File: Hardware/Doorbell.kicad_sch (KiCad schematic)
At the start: 57 parts, among them J1 Conn_02x05_Odd_Even, J2 MEM2051-00-195-00-A, J3 1935174, Q1 SIA517DJ-T1-GE3, Q2 DMP4047LFDE-7, U1 CD4052BPWRG3, U2 MAX98357AETE+T, U3 ATSAMG53N19B-AU, U4 VOS627A-X001T, U5 VOS627A-X001T, U6 MR25H128A

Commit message: Clean up custom KiCad libraries
- Clean up the directory structure for KiCad custom libraries.
- Fix paths in KiCad schematic and pcb for symbols, footprints, and
3d models for custom libraries.
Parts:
- F1, F2: footprint Libs:FUSE_4527 -> Fuse:FUSE_4527
- J1: footprint Libs:3220-10-0100-00 -> Connector:3220-10-0100-00
- J2: footprint Libs:MEM2051-00-195-00-A -> Connector:MEM2051-00-195-00-A
- Q2: footprint Libs:DMP4047LFDE-7 -> Transistor_SMD:DMP4047LFDE-7
- R10, R9: footprint Libs:35501K3FT -> Resistor_SMD:35501K3FT
- RV2: footprint Libs:PTV09A-4015U-B103 -> Potentiometer:PTV09A-4015U-B103
- U2: footprint Libs:MAX98357AETE_T -> IC:MAX98357AETE_T
- U3: footprint Libs:ATSAMG53N19B-AU -> IC:ATSAMG53N19B-AU
- U4, U5: footprint Libs:VOS627A-X001T -> IC:VOS627A-X001T

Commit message: Cleanup custom KiCad libraries
- Delete unneeded/unused files
- Cleanup symbol library files for custom libraries
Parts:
- J2: symbol MEM2051-00-195-00-A:MEM2051-00-195-00-A -> Doorbell_Connector:MEM2051-00-195-00-A
- Q1: symbol SIA517DJ-T1-GE3:SIA517DJ-T1-GE3 -> Doorbell_Transistor_SMD:SIA517DJ-T1-GE3
- Q2: symbol DMP4047LFDE-7:DMP4047LFDE-7 -> Doorbell_Transistor_SMD:DMP4047LFDE-7
- RV2: symbol PTV09A-4015U-B103:PTV09A-4015U-B103 -> Doorbell_Potentiometer:PTV09A-4015U-B103
- U1: symbol CD4052BPWRG3:CD4052BPWRG3 -> Doorbell_IC:CD4052BPWRG3
- U2: symbol MAX98357AETE_T:MAX98357AETE+T -> Doorbell_IC:MAX98357AETE+T
- U3: symbol ATSAMG53N19B-AU:ATSAMG53N19B-AU -> Doorbell_IC:ATSAMG53N19B-AU
- U4, U5: symbol VOS627A-X001T:VOS627A-X001T -> Doorbell_IC:VOS627A-X001T
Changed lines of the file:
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@@
     (pin "2")
   )
-  (symbol (lib_id "MAX98357AETE_T:MAX98357AETE+T") (at 83.82 156.21 0) (unit 1)
+  (symbol (lib_id "Doorbell_IC:MAX98357AETE+T") (at 83.82 156.21 0) (unit 1)
     (in_bom yes) (on_board yes)
     (property "Reference" "U2" (id 0) (at 83.82 136.652 0))
@@
     (pin "2")
   )
-  (symbol (lib_id "SIA517DJ-T1-GE3:SIA517DJ-T1-GE3") (at 77.47 116.84 0) (mirror y) (unit 2)
+  (symbol (lib_id "Doorbell_Transistor_SMD:SIA517DJ-T1-GE3") (at 77.47 116.84 0) (mirror y) (unit 2)
     (in_bom yes) (on_board yes)
     (property "Reference" "Q1" (id 0) (at 74.803 115.6716 0)
@@
     (pin "5")
   )
-  (symbol (lib_id "SIA517DJ-T1-GE3:SIA517DJ-T1-GE3") (at 55.88 102.87 180) (unit 1)
+  (symbol (lib_id "Doorbell_Transistor_SMD:SIA517DJ-T1-GE3") (at 55.88 102.87 180) (unit 1)
     (in_bom yes) (on_board yes)
     (property "Reference" "Q1" (id 0) (at 53.213 101.7016 0)
@@
     (pin "1")
   )
-  (symbol (lib_id "CD4052BPWRG3:CD4052BPWRG3") (at 46.99 63.5 90) (unit 1)
+  (symbol (lib_id "Doorbell_IC:CD4052BPWRG3") (at 46.99 63.5 90) (unit 1)
     (in_bom yes) (on_board yes)
     (property "Reference" "U1" (id 0) (at 28.1178 62.3316 90)
@@
     (pin "2")
   )
-  (symbol (lib_id "ATSAMG53N19B-AU:ATSAMG53N19B-AU") (at 161.29 97.79 0) (unit 1)
+  (symbol (lib_id "Doorbell_IC:ATSAMG53N19B-AU") (at 161.29 97.79 0) (unit 1)
     (in_bom yes) (on_board yes)
     (property "Reference" "U3" (id 0) (at 161.29 43.5102 0)
@@
     (pin "1")
   )
-  (symbol (lib_id "MEM2051-00-195-00-A:MEM2051-00-195-00-A") (at 248.92 38.1 180) (unit 1)
+  (symbol (lib_id "Doorbell_Connector:MEM2051-00-195-00-A") (at 248.92 38.1 180) (unit 1)
     (in_bom yes) (on_board yes)
     (property "Reference" "J2" (id 0) (at 244.0178 18.6182 0))
@@
     (pin "9")
   )
-  (symbol (lib_id "PTV09A-4015U-B103:PTV09A-4015U-B103") (at 99.06 88.9 0) (unit 1)
+  (symbol (lib_id "Doorbell_Potentiometer:PTV09A-4015U-B103") (at 99.06 88.9 0) (unit 1)
     (in_bom yes) (on_board yes)
     (property "Reference" "RV2" (id 0) (at 97.5614 86.5886 0)
@@
     (pin "1")
   )
-  (symbol (lib_id "VOS627A-X001T:VOS627A-X001T") (at 214.63 157.48 180) (unit 1)
+  (symbol (lib_id "Doorbell_IC:VOS627A-X001T") (at 214.63 157.48 180) (unit 1)
     (in_bom yes) (on_board yes)
     (property "Reference" "U5" (id 0) (at 214.63 148.082 0))
@@
     (pin "4")
   )
-  (symbol (lib_id "VOS627A-X001T:VOS627A-X001T") (at 214.63 132.08 0) (mirror y) (unit 1)
+  (symbol (lib_id "Doorbell_IC:VOS627A-X001T") (at 214.63 132.08 0) (mirror y) (unit 1)
     (in_bom yes) (on_board yes)
     (property "Reference" "U4" (id 0) (at 214.63 122.682 0))
@@
     (pin "2")
   )
-  (symbol (lib_id "DMP4047LFDE-7:DMP4047LFDE-7") (at 58.42 24.13 90) (unit 1)
+  (symbol (lib_id "Doorbell_Transistor_SMD:DMP4047LFDE-7") (at 58.42 24.13 90) (unit 1)
     (in_bom yes) (on_board yes)
     (property "Reference" "Q2" (id 0) (at 58.42 15.4432 90))

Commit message: Switch to local libraries for KiCad schematic
- Move all KiCad schematic symbols into local libraries
- Fix KiCad schematic library links to point to local libraries
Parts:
- BT1: symbol Device:Battery -> Doorbell_Battery:Battery
- C1, C10, C11, C12, C13, C14, C15, C16, C17, C18, C19, C2, C3, C4, C5, C6, C7, C8, C9: symbol Device:C_Small -> Doorbell_Capacitor:C_Small
- D1: symbol Device:D_Zener_Small -> Doorbell_Diode:D_Zener_Small
- D2: symbol Device:LED -> Doorbell_LED:LED
- F1, F2: symbol Device:Fuse_Small -> Doorbell_Fuse:Fuse_Small
- FB1, FB2: symbol Device:Ferrite_Bead_Small -> Doorbell_Inductor_SMD:FerriteBead_Small
- J1: value Conn_02x05_Odd_Even -> 3220-10-0100-00; symbol Connector_Generic:Conn_02x05_Odd_Even -> Doorbell_Connector:3220-10-0100-00
- J3: footprint TerminalBlock_Phoenix:TerminalBlock_Phoenix_PT-1,5-3-5.0-H_1x03_P5.00mm_Horizontal -> Connector:TerminalBlock_Phoenix_PT-1,5-3-5.0-H_1x03_P5.00mm_Horizontal; symbol Connector:Screw_Terminal_01x03 -> Doorbell_Connector:Screw_Terminal_01x03
- LS1: symbol Device:Speaker -> Doorbell_Speaker:Speaker
- R1, R10, R11, R12, R13, R14, R15, R2, R3, R4, R5, R6, R7, R8, R9: symbol Device:R_Small -> Doorbell_Resistor:R_Small
- RV1, RV3, RV4: symbol Device:Varistor -> Doorbell_Varistor:Varistor
- U6: symbol Memory_NVRAM:MR25H40 -> Doorbell_Memory:MR25H40

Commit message: Move KiCad global footprint and 3d models to local
- Move KiCad global footprint and 3d models to local directories
- Reassign footprints in KiCad schematic/PCB from global libraries to
  local libraries
- Reassign global 3d models to local 3d models for KiCad
- Update KiCad PCB with all local footprints
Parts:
- BT1, LS1: footprint Connector_Molex:Molex_MicroClasp_55935-0210_1x02_P2.00mm_Horizontal -> Connector:Molex_MicroClasp_55935-0210_1x02_P2.00mm_Horizontal
- Q1: footprint Package_TO_SOT_SMD:Vishay_PowerPAK_SC70-6L_Dual -> Transistor_SMD:Vishay_PowerPAK_SC70-6L_Dual
- U1: footprint Package_SO:TSSOP-16_4.4x5mm_P0.65mm -> IC:TSSOP-16_4.4x5mm_P0.65mm
- U6: footprint Package_DFN_QFN:DFN-8-1EP_6x5mm_P1.27mm_EP2x2mm -> IC:DFN-8-1EP_6x5mm_P1.27mm_EP2x2mm
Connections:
- new net: U2.12 (NC), U2.13 (NC), U2.5 (NC), U2.6 (NC)
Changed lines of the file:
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@@
     (pin "8")
     (pin "9")
+    (pin "12")
+    (pin "13")
+    (pin "5")
+    (pin "6")
   )
   (symbol (lib_id "Doorbell_Capacitor:C_Small") (at 114.3 148.59 0) (unit 1)
@@
       (effects (font (size 1.27 1.27)) (justify left))
     )
-    (property "Footprint" "Connector_Molex:Molex_MicroClasp_55935-0210_1x02_P2.00mm_Horizontal" (id 2) (at 162.56 177.8 0)
+    (property "Footprint" "Connector:Molex_MicroClasp_55935-0210_1x02_P2.00mm_Horizontal" (id 2) (at 162.56 177.8 0)
       (effects (font (size 1.27 1.27)) hide)
     )
@@
       (effects (font (size 1.27 1.27)) (justify left))
     )
-    (property "Footprint" "Package_TO_SOT_SMD:Vishay_PowerPAK_SC70-6L_Dual" (id 2) (at 78.74 128.905 0)
+    (property "Footprint" "Transistor_SMD:Vishay_PowerPAK_SC70-6L_Dual" (id 2) (at 78.74 128.905 0)
       (effects (font (size 1.27 1.27)) hide)
     )
@@
       (effects (font (size 1.27 1.27)) (justify left))
     )
-    (property "Footprint" "Package_TO_SOT_SMD:Vishay_PowerPAK_SC70-6L_Dual" (id 2) (at 57.15 90.805 0)
+    (property "Footprint" "Transistor_SMD:Vishay_PowerPAK_SC70-6L_Dual" (id 2) (at 57.15 90.805 0)
       (effects (font (size 1.27 1.27)) hide)
     )
@@
       (effects (font (size 1.27 1.27)) (justify left))
     )
-    (property "Footprint" "Package_SO:TSSOP-16_4.4x5mm_P0.65mm" (id 2) (at 66.04 59.69 0)
+    (property "Footprint" "IC:TSSOP-16_4.4x5mm_P0.65mm" (id 2) (at 66.04 59.69 0)
       (effects (font (size 1.27 1.27)) (justify left) hide)
     )
@@
       (effects (font (size 1.27 1.27)) (justify left))
     )
-    (property "Footprint" "Connector_Molex:Molex_MicroClasp_55935-0210_1x02_P2.00mm_Horizontal" (id 2) (at 26.924 21.59 90)
+    (property "Footprint" "Connector:Molex_MicroClasp_55935-0210_1x02_P2.00mm_Horizontal" (id 2) (at 26.924 21.59 90)
       (effects (font (size 1.27 1.27)) hide)
     )
@@
     (property "Reference" "U6" (id 0) (at 250.19 58.9026 0))
     (property "Value" "MR25H128A" (id 1) (at 250.19 61.214 0))
-    (property "Footprint" "Package_DFN_QFN:DFN-8-1EP_6x5mm_P1.27mm_EP2x2mm" (id 2) (at 250.19 73.66 0)
+    (property "Footprint" "IC:DFN-8-1EP_6x5mm_P1.27mm_EP2x2mm" (id 2) (at 250.19 73.66 0)
       (effects (font (size 1.27 1.27)) hide)
     )
@@
     )
     (path "/00000000-0000-0000-0000-0000643f25be"
-      (reference "BT1") (unit 1) (value "6xAA") (footprint "Connector_Molex:Molex_MicroClasp_55935-0210_1x02_P2.00mm_Horizontal")
+      (reference "BT1") (unit 1) (value "6xAA") (footprint "Connector:Molex_MicroClasp_55935-0210_1x02_P2.00mm_Horizontal")
     )
     (path "/00000000-0000-0000-0000-00006195168d"
@@
     )
     (path "/00000000-0000-0000-0000-00006434f40f/00000000-0000-0000-0000-0000643d3326"
-      (reference "D6") (unit 1) (value "V3FM12-M3/H") (footprint "Diode_SMD:D_SMF")
+      (reference "D6") (unit 1) (value "V3FM12-M3/H") (footprint "Diode_SMD:V3FM12-M3_H")
     )
     (path "/00000000-0000-0000-0000-0000665129d9/00000000-0000-0000-0000-00006651647e"
@@
     )
     (path "/00000000-0000-0000-0000-0000619771f5"
-      (reference "LS1") (unit 1) (value "Speaker") (footprint "Connector_Molex:Molex_MicroClasp_55935-0210_1x02_P2.00mm_Horizontal")
+      (reference "LS1") (unit 1) (value "Speaker") (footprint "Connector:Molex_MicroClasp_55935-0210_1x02_P2.00mm_Horizontal")
     )
     (path "/00000000-0000-0000-0000-000061acc594"
-      (reference "Q1") (unit 1) (value "SIA517DJ-T1-GE3") (footprint "Package_TO_SOT_SMD:Vishay_PowerPAK_SC70-6L_Dual")
+      (reference "Q1") (unit 1) (value "SIA517DJ-T1-GE3") (footprint "Transistor_SMD:Vishay_PowerPAK_SC70-6L_Dual")
     )
     (path "/00000000-0000-0000-0000-000061ac7063"
-      (reference "Q1") (unit 2) (value "SIA517DJ-T1-GE3") (footprint "Package_TO_SOT_SMD:Vishay_PowerPAK_SC70-6L_Dual")
+      (reference "Q1") (unit 2) (value "SIA517DJ-T1-GE3") (footprint "Transistor_SMD:Vishay_PowerPAK_SC70-6L_Dual")
     )
     (path "/00000000-0000-0000-0000-0000675a9d90"
@@
     )
     (path "/00000000-0000-0000-0000-00006434f40f/00000000-0000-0000-0000-0000648f5004"
-      (reference "Q4") (unit 1) (value "BC847") (footprint "Package_TO_SOT_SMD:SOT-23")
+      (reference "Q4") (unit 1) (value "BC847") (footprint "Transistor_SMD:SOT-23")
     )
     (path "/00000000-0000-0000-0000-00006434f40f/00000000-0000-0000-0000-0000649028a0"
-      (reference "Q5") (unit 1) (value "BC847") (footprint "Package_TO_SOT_SMD:SOT-23")
+      (reference "Q5") (unit 1) (value "BC847") (footprint "Transistor_SMD:SOT-23")
     )
     (path "/00000000-0000-0000-0000-000061e3d0d7"
@@
     )
     (path "/00000000-0000-0000-0000-000061d6fed6"
-      (reference "U1") (unit 1) (value "CD4052BPWRG3") (footprint "Package_SO:TSSOP-16_4.4x5mm_P0.65mm")
+      (reference "U1") (unit 1) (value "CD4052BPWRG3") (footprint "IC:TSSOP-16_4.4x5mm_P0.65mm")
     )
     (path "/00000000-0000-0000-0000-00006194c427"
@@
     )
     (path "/00000000-0000-0000-0000-000066923e5d"
-      (reference "U6") (unit 1) (value "MR25H128A") (footprint "Package_DFN_QFN:DFN-8-1EP_6x5mm_P1.27mm_EP2x2mm")
+      (reference "U6") (unit 1) (value "MR25H128A") (footprint "IC:DFN-8-1EP_6x5mm_P1.27mm_EP2x2mm")
     )
     (path "/00000000-0000-0000-0000-00006434f40f/00000000-0000-0000-0000-000067503003"
@@
     )
     (path "/00000000-0000-0000-0000-00006434f40f/00000000-0000-0000-0000-00006757a4a0"
-      (reference "U9") (unit 1) (value "LM2903DR2G") (footprint "Package_SO:SOIC-8_3.9x4.9mm_P1.27mm")
+      (reference "U9") (unit 1) (value "LM2903DR2G") (footprint "IC:SOIC-8_3.9x4.9mm_P1.27mm")
     )
     (path "/00000000-0000-0000-0000-00006434f40f/00000000-0000-0000-0000-00006757cdae"
-      (reference "U9") (unit 2) (value "LM2903DR2G") (footprint "Package_SO:SOIC-8_3.9x4.9mm_P1.27mm")
+      (reference "U9") (unit 2) (value "LM2903DR2G") (footprint "IC:SOIC-8_3.9x4.9mm_P1.27mm")
     )
     (path "/00000000-0000-0000-0000-00006434f40f/00000000-0000-0000-0000-00006757d8fb"
-      (reference "U9") (unit 3) (value "LM2903DR2G") (footprint "Package_SO:SOIC-8_3.9x4.9mm_P1.27mm")
+      (reference "U9") (unit 3) (value "LM2903DR2G") (footprint "IC:SOIC-8_3.9x4.9mm_P1.27mm")
     )
     (path "/00000000-0000-0000-0000-00006434f40f/00000000-0000-0000-0000-0000643d32f2"
@@
     )
     (path "/00000000-0000-0000-0000-0000665129d9/00000000-0000-0000-0000-0000665164bb"
-      (reference "U11") (unit 1) (value "PI4IOE5V9535LEX") (footprint "Package_SO:TSSOP-24_4.4x7.8mm_P0.65mm")
-    )
-  )
+      (reference "U11") (unit 1) (value "PI4IOE5V9535LEX") (footprint "IC:TSSOP-24_4.4x7.8mm_P0.65mm")
+    )
+  )

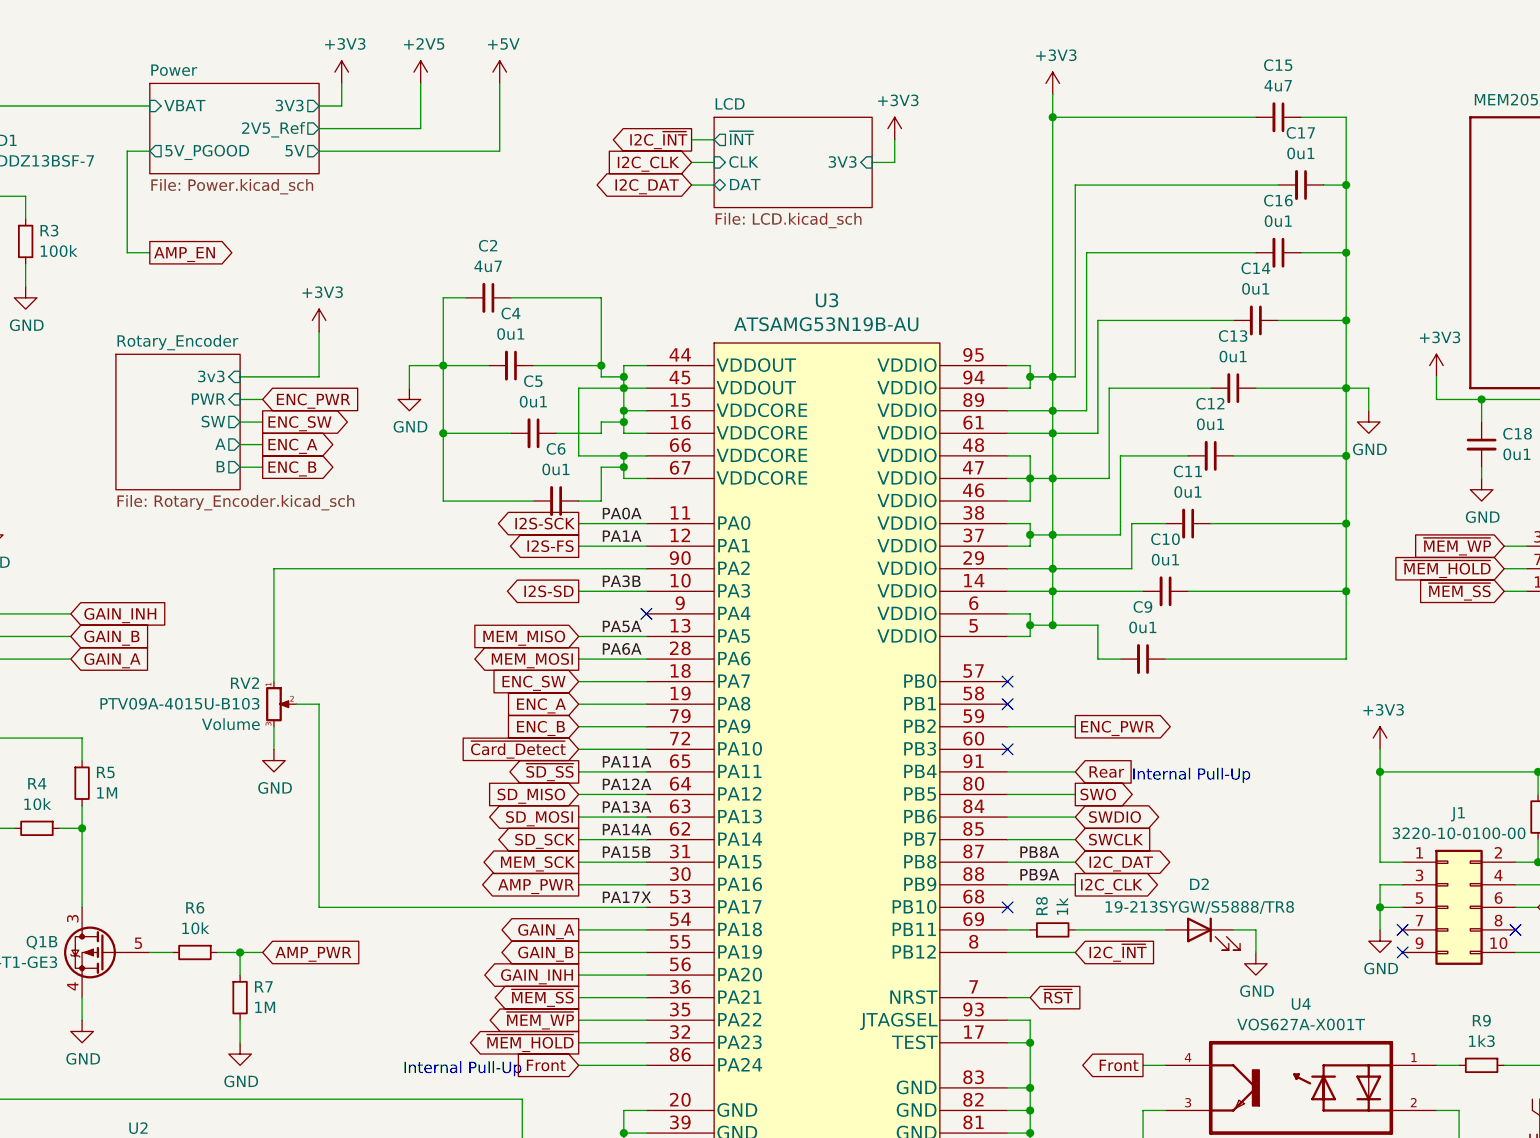
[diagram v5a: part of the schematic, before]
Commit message: Bump to board revision B
- Redesign low battery circuit
	- Replace comparator with PMIC
	- Utilize LED Driver IC
	- Remove unneeded 2.5v voltage reference
- Reroute some signals onto wkup/external interrupt pins
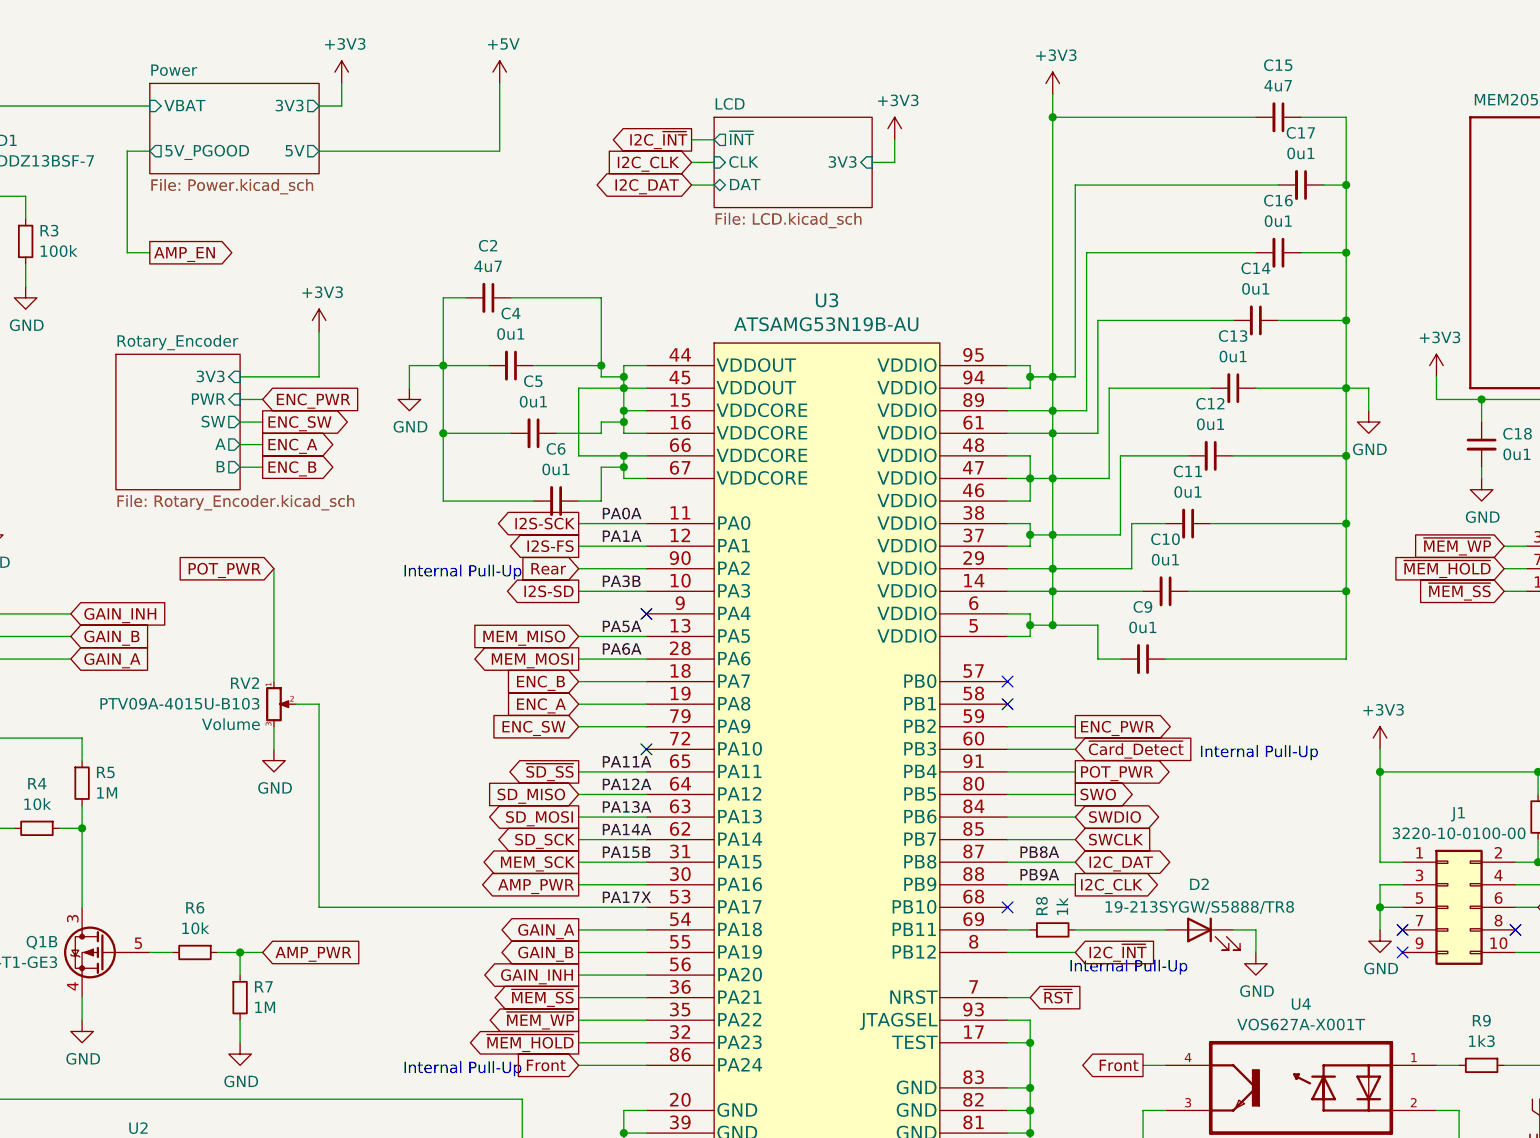
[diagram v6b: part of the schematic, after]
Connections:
- net ENC_B: now also U3.18 (PA7); no longer U3.79 (PA9)
- net ENC_SW: now also U3.79 (PA9); no longer U3.18 (PA7)
- net Rear: now also U3.90 (PA2); no longer U3.91 (PB4)
- net ~{Card_Detect}: now also U3.60 (PB3); no longer U3.72 (PA10)
- net POT_PWR: now reaches RV2.1
- net POT_PWR: now also U3.91 (PB4); no longer U3.90 (PA2)
- now unconnected: U2.12 (NC), U2.13 (NC), U2.5 (NC), U2.6 (NC)
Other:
- sheet Power ports: added none; removed 2V5_Ref
- sheet Rotary_Encoder ports: added 3V3; removed 3v3
